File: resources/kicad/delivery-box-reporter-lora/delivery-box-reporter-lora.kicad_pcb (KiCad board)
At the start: 2 copper layers, 70.8 x 74.6 mm, 15 parts, among them J1 Power 4v-6v, Q2 2N3904, U1 ESP8266 D1 Mini, U4 TLV803EB33VDBZR, U5 MCP1702-3302E, U7 WeMos_D1_mini

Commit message: Mostly changes to the box and board design
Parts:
- J1: value Power 4v-6v -> Solar Power 4v-6v
- moved U7 5.07 mm to (90.8, 78.9)
- moved U8 5.07 mm to (107.3, 66.3)
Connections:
- U6 pad 1: +3.3V -> Earth
- U6 pad 2: unconnected-(U6-RST-Pad2) -> /SS RX
- U6 pad 4: /SS RX -> unconnected-(U6-RST-Pad4)
- U6 pad 5: Earth -> +3.3V
- U8 pad 1: /Receiver/3v3B -> Net-(U7-GND)
- U8 pad 2: unconnected-(U8-RST-Pad2) -> /Receiver/SS RX
- U8 pad 4: /Receiver/SS RX -> unconnected-(U8-RST-Pad4)
- U8 pad 5: Net-(U7-GND) -> /Receiver/3v3B
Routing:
- net +3.3V: track 175.8 -> 145.9 mm
- net Earth: track 140.0 -> 160.0 mm
- net /Receiver/SS TX: track 27.5 -> 35.7 mm
- net Net-(U7-GND): track 42.9 -> 35.7 mm
- net /SS TX: track 38.0 -> 34.1 mm
- net /Receiver/3v3B: track 37.2 -> 39.5 mm
- net /Receiver/SS RX: track 23.9 -> 26.0 mm
- net /SS RX: track 34.5 -> 35.2 mm
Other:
- board size 70.8 x 74.6 mm -> 75.9 x 74.6 mm
- board text added: "Receiver Delivery Box Reporter Version 2.1.0 2-3-25 David E. Powell"
- board text added: "Sensor Delivery Box Reporter Version 2.1.0 2-3-25 David E. Powell"
- board text removed: "Receiver Delivery Box Reporter Version 2.0.1 1-11-25 David E. Powell"
- board text removed: "Sensor Delivery Box Reporter Version 2.0.1 1-11-25 David E. Powell"

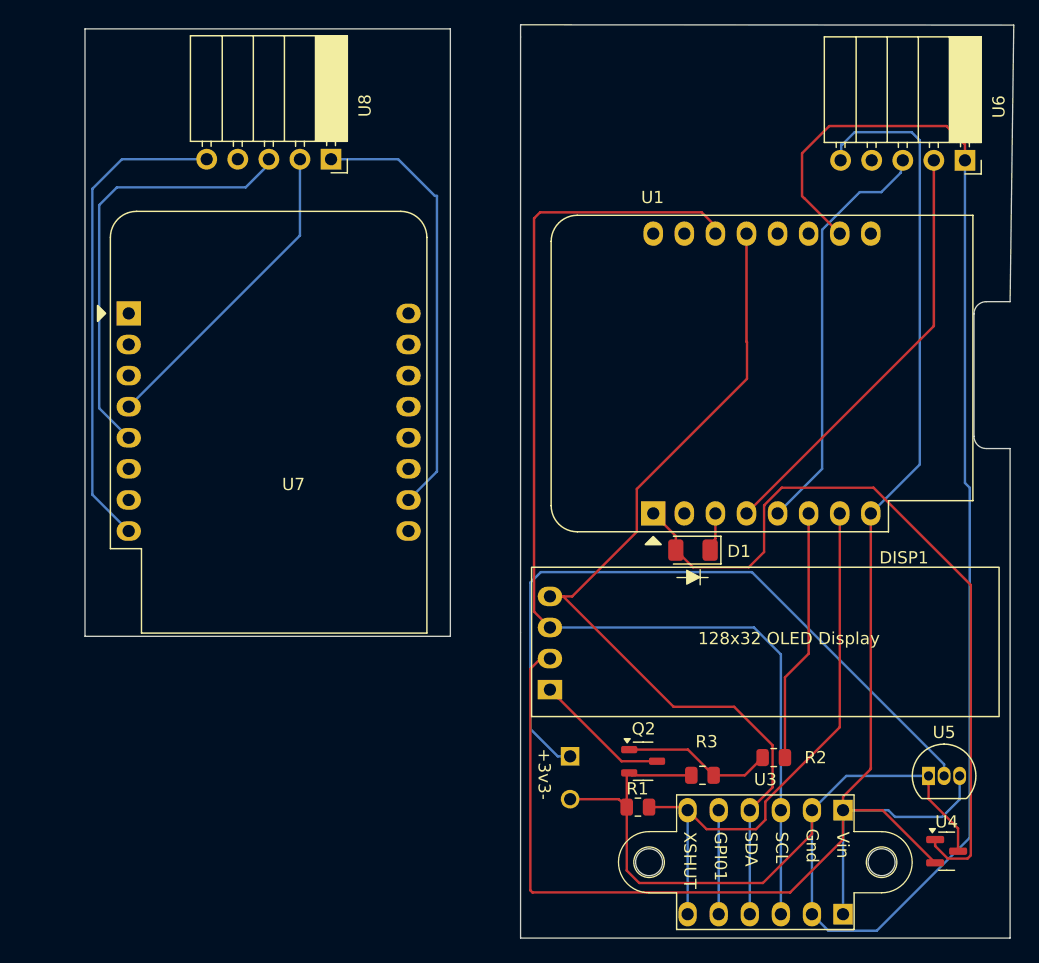
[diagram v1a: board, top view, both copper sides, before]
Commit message: Changes to the enclosures, presentation, and code
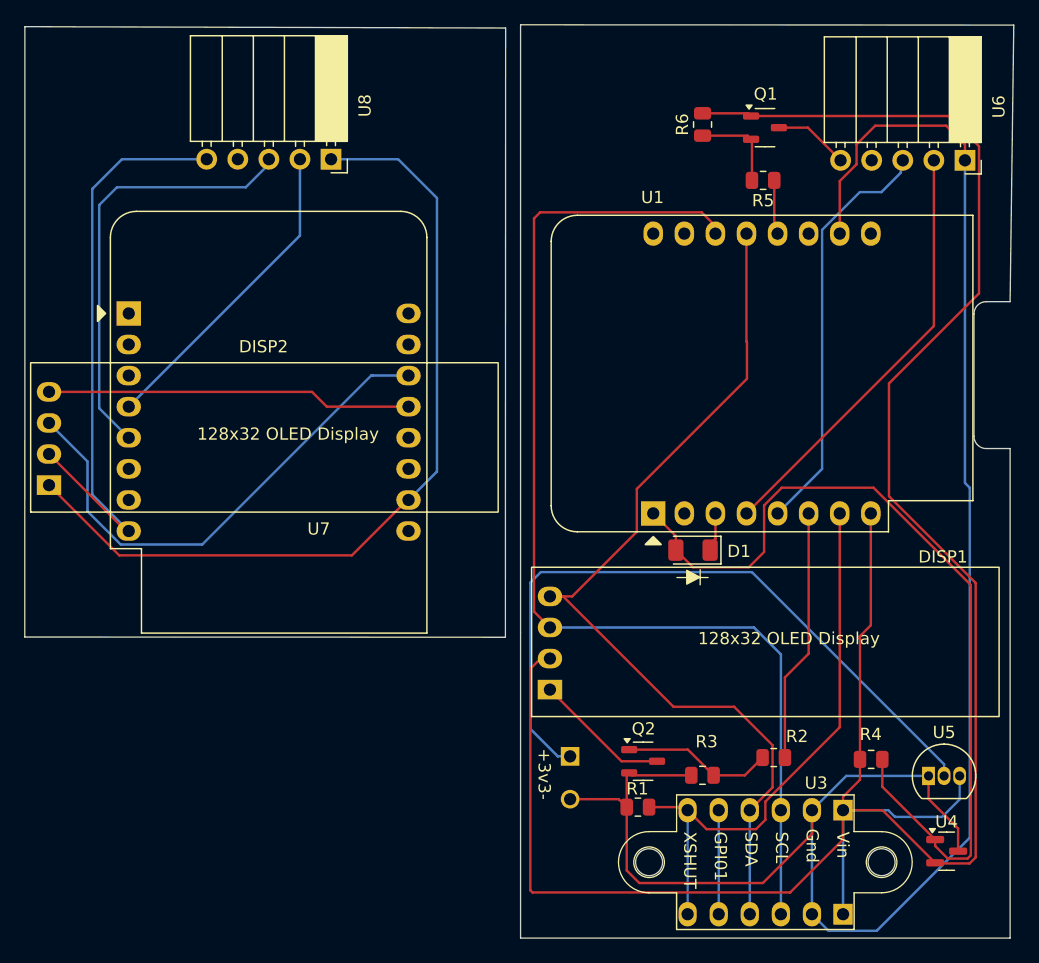
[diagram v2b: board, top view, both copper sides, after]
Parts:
- added DISP2: 128x32_OLED_Display, Davids_Footprints:OLED_0.91_128x32, F.Cu at (84.2, 92.9)
- added Q1: 2N3906, Davids_Footprints:MMBT3904-7-F_SOT-23-3, F.Cu at (142.8, 63.7)
- added R4: 10K, Resistor_SMD:R_0805_2012Metric, F.Cu at (151.4, 115.3)
- added R5: 10K, Resistor_SMD:R_0805_2012Metric, F.Cu at (142.6, 68.0)
- added R6: 10K, Resistor_SMD:R_0805_2012Metric, F.Cu at (137.7, 63.4)
- U4: value TLV803EB33VDBZR -> TLV803EA30VDBZR
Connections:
- U1 pad 12: unconnected-(U1-D3-Pad12) -> /LoRa En
- U6 pad 5: +3.3V -> Net-(Q1-C)
- U7 pad 13: unconnected-(U7-SDA/D2-Pad13) -> Net-(DISP2-SDA)
- U7 pad 14: unconnected-(U7-SCL/D1-Pad14) -> Net-(DISP2-SCL)
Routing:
- net +3.3V: track 145.9 -> 196.1 mm
- net Net-(DISP2-SCL): track 0.00 -> 41.6 mm
- net Net-(DISP2-Gnd): track 35.7 -> 69.2 mm
- net Net-(DISP2-SDA): track 0.00 -> 29.9 mm
- net /Receiver/3v3B: track 39.5 -> 48.7 mm
- net Net-(D1-A): track 62.7 -> 71.1 mm
- net Net-(Q1-B): track 0.00 -> 7.48 mm
- net Net-(Q1-C): track 0.00 -> 6.15 mm
- net Earth: track 160.0 -> 155.2 mm
- net /LoRa En: track 0.00 -> 4.46 mm
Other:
- board size 75.9 x 74.6 mm -> 80.8 x 74.6 mm
- board text added: "Receiver Delivery Box Reporter Version 2.2.0 2-10-25 David E. Powell"
- board text added: "Sensor Delivery Box Reporter Version 2.2.0 2-10-25 David E. Powell"
- board text removed: "Receiver Delivery Box Reporter Version 2.1.0 2-3-25 David E. Powell"
- board text removed: "Sensor Delivery Box Reporter Version 2.1.0 2-3-25 David E. Powell"

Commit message: Small changes to the LoRa power circuit.
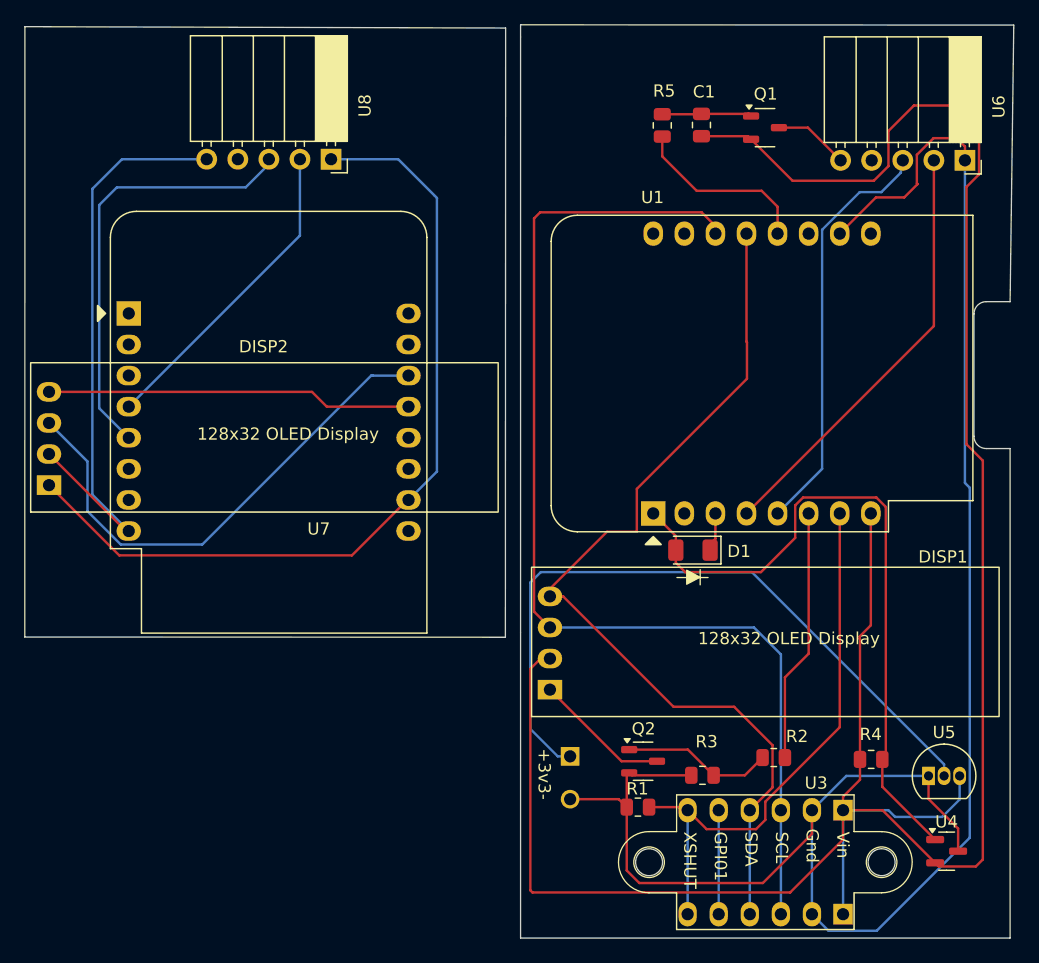
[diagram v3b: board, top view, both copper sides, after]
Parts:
- removed R6: 10K, Resistor_SMD:R_0805_2012Metric
- added C1: 22 μF, Resistor_SMD:R_0805_2012Metric, F.Cu at (137.6, 63.5)
- R5: value 10K -> 1K
- moved R5 9.38 mm to (134.4, 63.5), turned to 90 degrees
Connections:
- Q1 pad 1: +3.3V -> Net-(Q1-B)
- Q1 pad 2: Net-(Q1-B) -> +3.3V
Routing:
- net Net-(D1-A): track 71.1 -> 55.0 mm
- net /LoRa En: track 4.46 -> 15.3 mm
- net +3.3V: track 196.1 -> 200.5 mm
- net Earth: track 155.2 -> 152.3 mm
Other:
- board text added: "Receiver Delivery Box Reporter Version 2.2.1 3-4-25 David E. Powell"
- board text added: "Sensor Delivery Box Reporter Version 2.2.1 3-4-25 David E. Powell"
- board text removed: "Receiver Delivery Box Reporter Version 2.2.0 2-10-25 David E. Powell"
- board text removed: "Sensor Delivery Box Reporter Version 2.2.0 2-10-25 David E. Powell"
